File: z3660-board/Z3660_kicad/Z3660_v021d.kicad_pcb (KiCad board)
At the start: 4 copper layers, 173.9 x 92.8 mm, 178 parts, among them CN1 KEL-8817-200-170S-F, CN2 Conn_02x40_Odd_Even, CN3 Conn_02x40_Odd_Even, J1 Jumper_2_Open, J2 Conn_02x07_Odd_Even, U1 LTC2990, U10 74FCT543A, U11 74FCT543A, U12 74FCT543A, U13 74FCT543A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

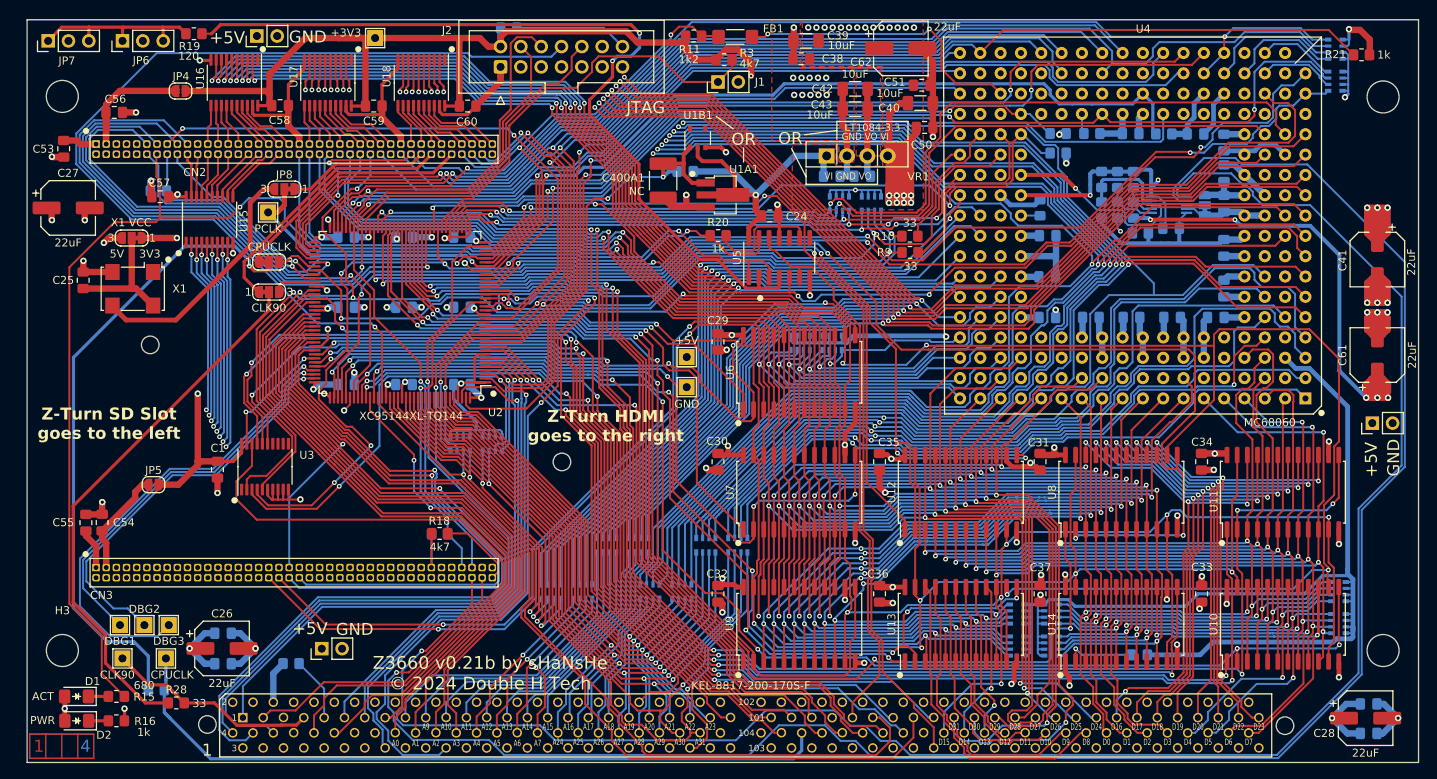
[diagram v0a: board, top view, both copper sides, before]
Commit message: Update to PCB v0.21d Minor change in footprint of fans
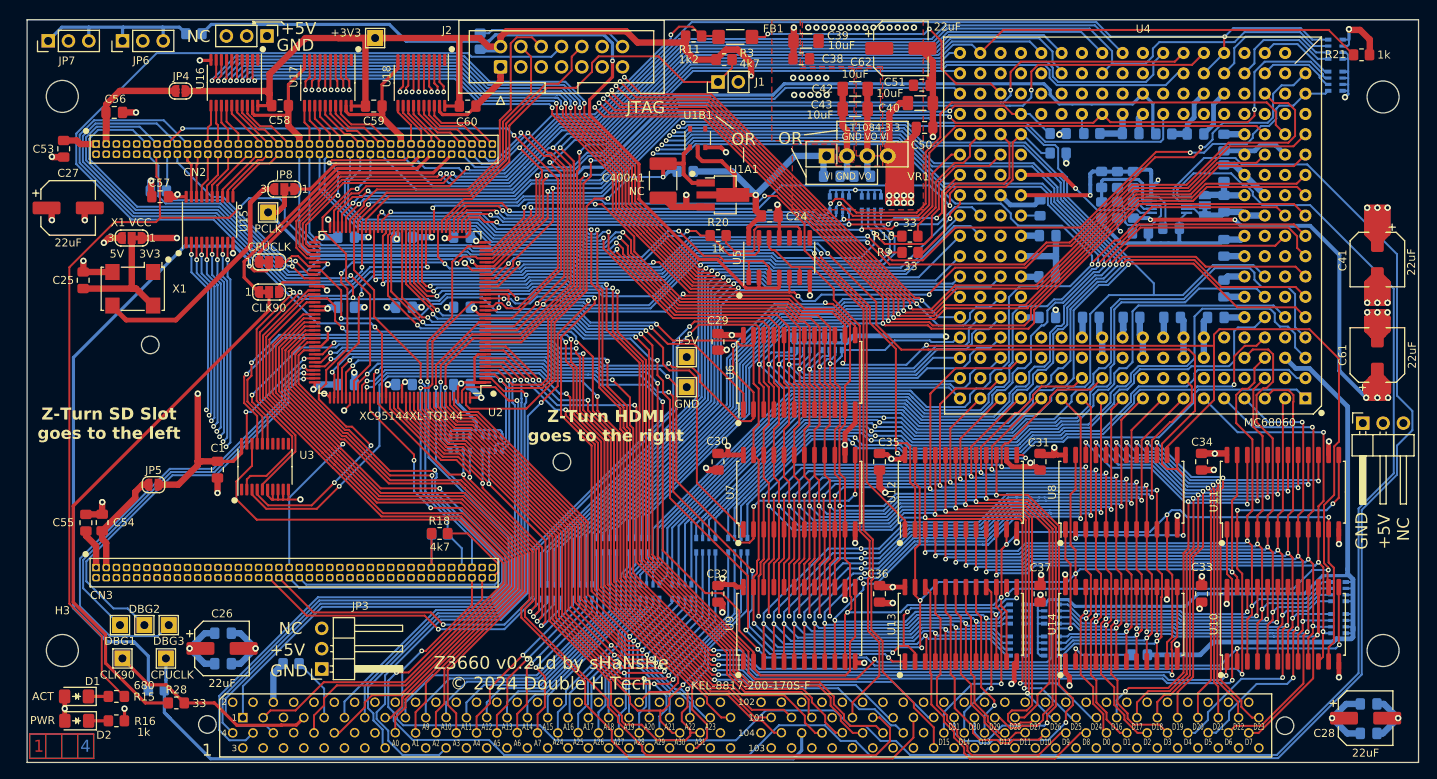
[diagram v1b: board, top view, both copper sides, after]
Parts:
- JP1, JP3: footprint Z3660_v02:PinHeader_1x02_P2.54mm_Vertical -> Z3660_v02:PinHeader_1x03_P2.54mm_Horizontal
- JP2: footprint Z3660_v02:PinHeader_1x02_P2.54mm_Vertical -> Z3660_v02:PinHeader_1x03_P2.54mm_Vertical
- R19: moved to B.Cu
- moved R4 3.93 mm to (136.9, 32.4), turned to 90 degrees
- moved JP1 1.35 mm to (249.8, 80.1), turned to -90 degrees
- moved JP2 1.27 mm to (110.3, 31.8), turned to -90 degrees
- turned JP3 to 0 degrees
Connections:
- JP1 pad 1: +5V -> Earth
- JP1 pad 2: Earth -> +5V
- JP2 pad 1: +5V -> Earth
- JP2 pad 2: Earth -> +5V
- JP3 pad 1: +5V -> Earth
- JP3 pad 2: Earth -> +5V
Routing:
- net Net-(R19-Pad1): track 107.3 -> 101.4 mm, vias 2 -> 1
- net Net-(J2-Pin_14): track 14.2 -> 18.8 mm
- net I2C0_SDA: track 238.0 -> 237.2 mm
- net I2C0_CLK: track 246.7 -> 247.5 mm
- net +3V3: track 493.4 -> 494.0 mm
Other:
- board text added: "NC"
- board text added: "Z3660 v0.21d by sHaNsHe © 2024 Double H Tech"
- board text removed: "Z3660 v0.21b by sHaNsHe © 2024 Double H Tech"
